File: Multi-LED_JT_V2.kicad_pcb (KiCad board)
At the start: 2 copper layers, 54.1 x 14.5 mm, 11 parts, among them Q1 BC817-25

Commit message: add DPDT switch
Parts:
- added SW1: SW_DPDT, lib_fp:DPDT_JS202011JAQN, F.Cu at (233.3, 117.7)
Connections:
- BT1 pad 2: GND -> Net-(BT1-Pad2)
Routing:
- net GND: track 62.9 -> 58.1 mm
- net Net-(BT1-Pad2): track 0.00 -> 4.10 mm
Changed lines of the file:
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@@
 (kicad_pcb (version 4) (host pcbnew 4.0.7)
   (general
-    (links 18)
+    (links 19)
     (no_connects 0)
-    (area 185.474999 105.574999 239.725001 120.225001)
+    (area 185.474999 104.925 239.725001 120.225001)
     (thickness 1.6)
     (drawings 6)
-    (tracks 62)
+    (tracks 64)
     (zones 0)
-    (modules 11)
-    (nets 6)
+    (modules 12)
+    (nets 8)
   )
   (page A4)
@@
     (mod_text_size 1 1)
     (mod_text_width 0.15)
-    (pad_size 2.794 2.794)
-    (pad_drill 1.778)
+    (pad_size 0.9 0.9)
+    (pad_drill 0.9)
     (pad_to_mask_clearance 0.2)
     (aux_axis_origin 0 0)
@@
   (net 4 "Net-(L1-Pad4)")
   (net 5 "Net-(Q1-Pad1)")
+  (net 6 "Net-(BT1-Pad2)")
+  (net 7 "Net-(SW1-Pad1)")
   (net_class Default "This is the default net class."
     (clearance 0.2)
@@
     (add_net GND)
     (add_net "Net-(BT1-Pad1)")
+    (add_net "Net-(BT1-Pad2)")
     (add_net "Net-(D1-Pad2)")
     (add_net "Net-(L1-Pad4)")
     (add_net "Net-(Q1-Pad1)")
+    (add_net "Net-(SW1-Pad1)")
   )
   (module AA_PCB-Clip (layer B.Cu)
@@
     (pad 2 thru_hole circle (at 33.528 0) (size 2.794 2.794) (drill 1.778) (layers *.Cu *.Mask B.SilkS))
     (pad 2 thru_hole circle (at 41.148 0) (size 2.794 2.794) (drill 1.778) (layers *.Cu *.Mask B.SilkS)
-      (net 2 GND))
+      (net 6 "Net-(BT1-Pad2)"))
   )
   (module lib_fp:LED_Luminus_MP-2016 (layer F.Cu)
@@
       (xy 2.975 -8.625)) (layer B.SilkS) (width 0.01))
   )
+  (module lib_fp:DPDT_JS202011JAQN (layer F.Cu)
+    (at 233.3 117.7)
+    (fp_text reference SW1 (at 0.1 -2.8) (layer F.SilkS)
+      (effects (font (size 1 1) (thickness 0.15)))
+    )
+    (fp_text value SW_DPDT (at 0 0) (layer F.Fab)
+      (effects (font (size 1 1) (thickness 0.15)))
+    )
+    (pad 1 smd rect (at -2.5 -1.2) (size 1 1.6) (layers F.Cu F.Paste F.Mask)
+      (net 7 "Net-(SW1-Pad1)"))
+    (pad 2 smd rect (at 0 -1.2) (size 1 1.6) (layers F.Cu F.Paste F.Mask)
+      (net 2 GND))
+    (pad 3 smd rect (at 2.5 -1.2) (size 1 1.6) (layers F.Cu F.Paste F.Mask)
+      (net 6 "Net-(BT1-Pad2)"))
+    (pad 4 smd rect (at -2.5 1.2) (size 1 1.6) (layers F.Cu F.Paste F.Mask))
+    (pad 5 smd rect (at 0 1.2) (size 1 1.6) (layers F.Cu F.Paste F.Mask))
+    (pad 6 smd rect (at 2.5 1.2) (size 1 1.6) (layers F.Cu F.Paste F.Mask))
+    (pad "" np_thru_hole circle (at -3.4 0) (size 0.9 0.9) (drill 0.9) (layers *.Cu *.Mask))
+    (pad "" np_thru_hole circle (at 3.4 0) (size 0.9 0.9) (drill 0.9) (layers *.Cu *.Mask))
+  )
   (gr_text "1.5V AA (LR6)" (at 212.8 117.5) (layer B.SilkS)
     (effects (font (size 1 1) (thickness 0.1)) (justify mirror))
@@
   (segment (start 186.5 112.7) (end 186.5 108.8) (width 0.25) (layer F.Cu) (net 1))
   (segment (start 186.7 112.9) (end 186.5 112.7) (width 0.25) (layer F.Cu) (net 1))
+  (segment (start 228 115.3) (end 233 115.3) (width 0.25) (layer F.Cu) (net 2))
+  (segment (start 224.4 115.3) (end 228 115.3) (width 0.25) (layer F.Cu) (net 2))
+  (segment (start 233.3 115.6) (end 233.3 116.5) (width 0.25) (layer F.Cu) (net 2))
+  (segment (start 233 115.3) (end 233.3 115.6) (width 0.25) (layer F.Cu) (net 2))
   (segment (start 200.2 115.3) (end 193.2 115.3) (width 0.25) (layer F.Cu) (net 2))
   (segment (start 192.95 115.05) (end 192.95 113.6) (width 0.25) (layer F.Cu) (net 2))
@@
   (segment (start 219.125 115.025) (end 219.125 112.9) (width 0.25) (layer F.Cu) (net 2))
   (segment (start 219.4 115.3) (end 219.125 115.025) (width 0.25) (layer F.Cu) (net 2))
-  (segment (start 236.998 112.9) (end 236.998 114.802) (width 0.25) (layer F.Cu) (net 2))
   (segment (start 223.925 114.825) (end 223.925 112.9) (width 0.25) (layer F.Cu) (net 2))
   (segment (start 224.4 115.3) (end 223.925 114.825) (width 0.25) (layer F.Cu) (net 2))
-  (segment (start 236.5 115.3) (end 228.8 115.3) (width 0.25) (layer F.Cu) (net 2))
-  (segment (start 228.8 115.3) (end 224.4 115.3) (width 0.25) (layer F.Cu) (net 2))
-  (segment (start 236.998 114.802) (end 236.5 115.3) (width 0.25) (layer F.Cu) (net 2))
   (segment (start 220.525 109.725) (end 225.125 109.725) (width 0.25) (layer F.Cu) (net 3))
   (segment (start 225.65 110.25) (end 225.65 112.9) (width 0.25) (layer F.Cu) (net 3))
@@
   (segment (start 190.4 111) (end 188.8 111) (width 0.25) (layer F.Cu) (net 5))
   (segment (start 191.05 111.65) (end 190.4 111) (width 0.25) (layer F.Cu) (net 5))
+  (segment (start 235.8 116.5) (end 235.8 114.098) (width 0.25) (layer F.Cu) (net 6))
+  (segment (start 235.8 114.098) (end 236.998 112.9) (width 0.25) (layer F.Cu) (net 6))
 )

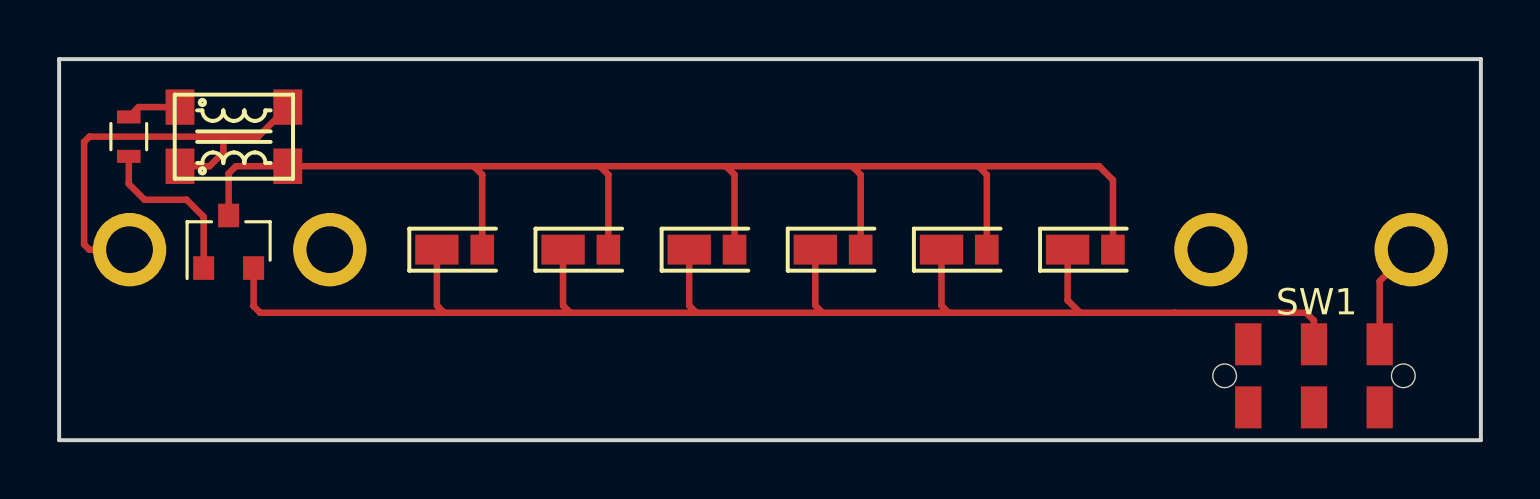
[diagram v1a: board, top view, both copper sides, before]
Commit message: no net fill back and front
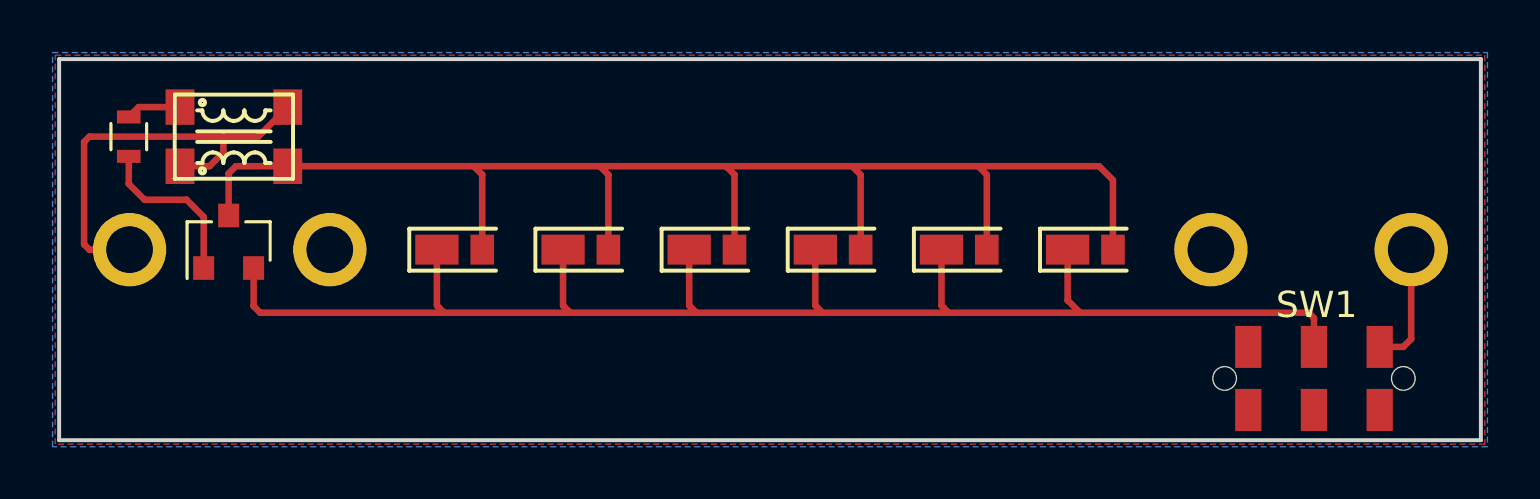
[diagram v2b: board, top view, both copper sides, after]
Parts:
- moved SW1 0.10 mm to (233.3, 117.8)
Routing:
- net Net-(BT1-Pad2): track 4.10 -> 4.72 mm
- added copper zone on B.Cu, net (none)
- added copper zone on F.Cu, net (none)
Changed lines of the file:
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@@
     (links 19)
     (no_connects 0)
-    (area 185.474999 104.925 239.725001 120.225001)
+    (area 185.474999 105.574999 239.725001 120.225001)
     (thickness 1.6)
     (drawings 6)
@@
   )
   (module lib_fp:DPDT_JS202011JAQN (layer F.Cu)
-    (at 233.3 117.7)
+    (at 233.3 117.8)
     (fp_text reference SW1 (at 0.1 -2.8) (layer F.SilkS)
       (effects (font (size 1 1) (thickness 0.15)))
@@
   (segment (start 186.5 112.7) (end 186.5 108.8) (width 0.25) (layer F.Cu) (net 1))
   (segment (start 186.7 112.9) (end 186.5 112.7) (width 0.25) (layer F.Cu) (net 1))
-  (segment (start 228 115.3) (end 233 115.3) (width 0.25) (layer F.Cu) (net 2))
-  (segment (start 224.4 115.3) (end 228 115.3) (width 0.25) (layer F.Cu) (net 2))
-  (segment (start 233.3 115.6) (end 233.3 116.5) (width 0.25) (layer F.Cu) (net 2))
-  (segment (start 233 115.3) (end 233.3 115.6) (width 0.25) (layer F.Cu) (net 2))
+  (segment (start 224.4 115.3) (end 233.1 115.3) (width 0.25) (layer F.Cu) (net 2))
+  (segment (start 233.3 115.5) (end 233.3 116.6) (width 0.25) (layer F.Cu) (net 2) (status 800000))
+  (segment (start 233.1 115.3) (end 233.3 115.5) (width 0.25) (layer F.Cu) (net 2))
   (segment (start 200.2 115.3) (end 193.2 115.3) (width 0.25) (layer F.Cu) (net 2))
   (segment (start 192.95 115.05) (end 192.95 113.6) (width 0.25) (layer F.Cu) (net 2))
@@
   (segment (start 190.4 111) (end 188.8 111) (width 0.25) (layer F.Cu) (net 5))
   (segment (start 191.05 111.65) (end 190.4 111) (width 0.25) (layer F.Cu) (net 5))
-  (segment (start 235.8 116.5) (end 235.8 114.098) (width 0.25) (layer F.Cu) (net 6))
-  (segment (start 235.8 114.098) (end 236.998 112.9) (width 0.25) (layer F.Cu) (net 6))
+  (segment (start 235.8 116.6) (end 236.7 116.6) (width 0.25) (layer F.Cu) (net 6) (status 400000))
+  (segment (start 236.998 116.302) (end 236.998 112.9) (width 0.25) (layer F.Cu) (net 6) (status 800000))
+  (segment (start 236.7 116.6) (end 236.998 116.302) (width 0.25) (layer F.Cu) (net 6))
+  (zone (net 0) (net_name "") (layer F.Cu) (hatch edge 0.508)
+    (connect_pads (clearance 0.381))
+    (min_thickness 0.127)
+    (fill yes (arc_segments 16) (thermal_gap 0.254) (thermal_bridge_width 0.762))
+    (polygon
+      (pts
+        (xy 239.8 120.3) (xy 185.4 120.3) (xy 185.4 105.5) (xy 239.8 105.5)
+      )
+    )
+  )
+  (zone (net 0) (net_name "") (layer B.Cu) (hatch edge 0.508)
+    (connect_pads (clearance 0.381))
+    (min_thickness 0.127)
+    (fill yes (arc_segments 16) (thermal_gap 0.254) (thermal_bridge_width 0.762))
+    (polygon
+      (pts
+        (xy 239.9 120.4) (xy 185.3 120.4) (xy 185.3 105.4) (xy 239.9 105.4)
+      )
+    )
+  )
 )
